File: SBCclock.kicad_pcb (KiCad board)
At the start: 4 copper layers, 37.5 x 23.4 mm, 20 parts, among them J1 Conn_01x07, J2 Conn_01x07, U1 74HCT14, U2 74HCT163, U3 74HCT112, U5 74HCT153, Y1 25.175MHz

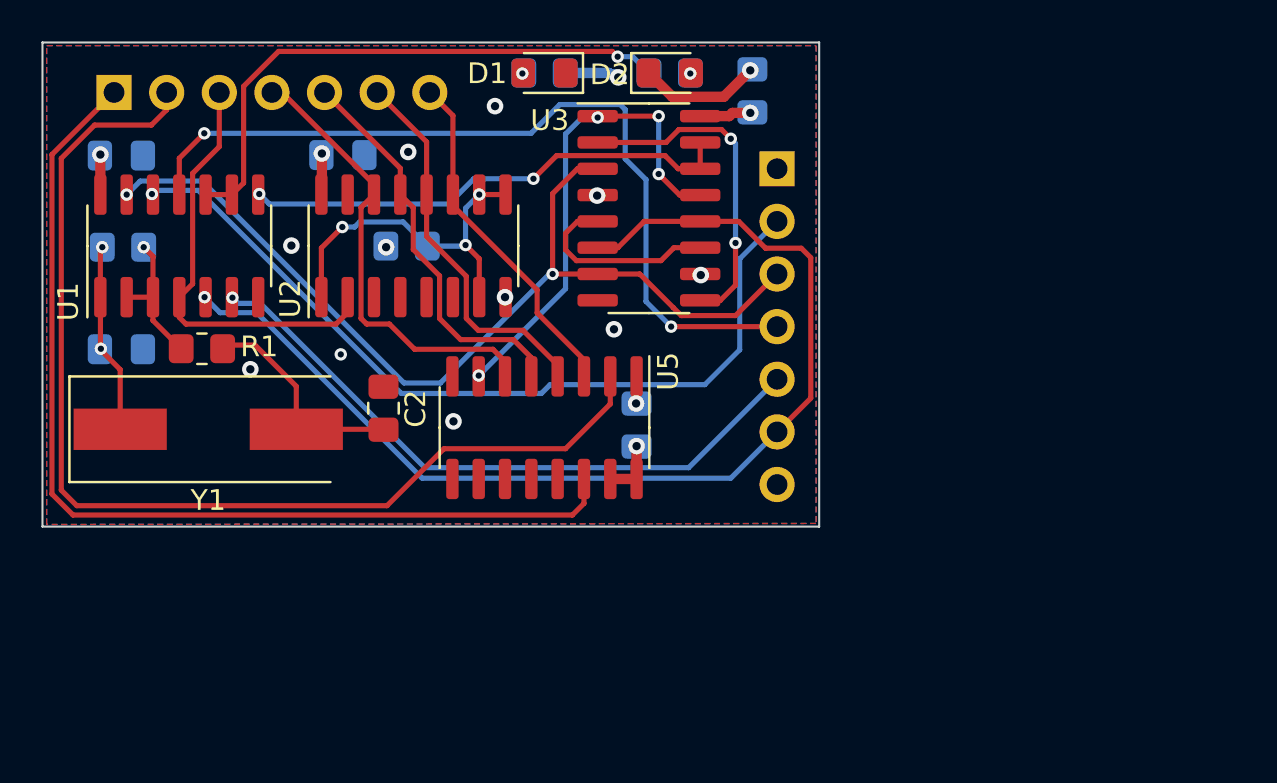
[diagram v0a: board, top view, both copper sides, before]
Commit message: reinforce clock outputs
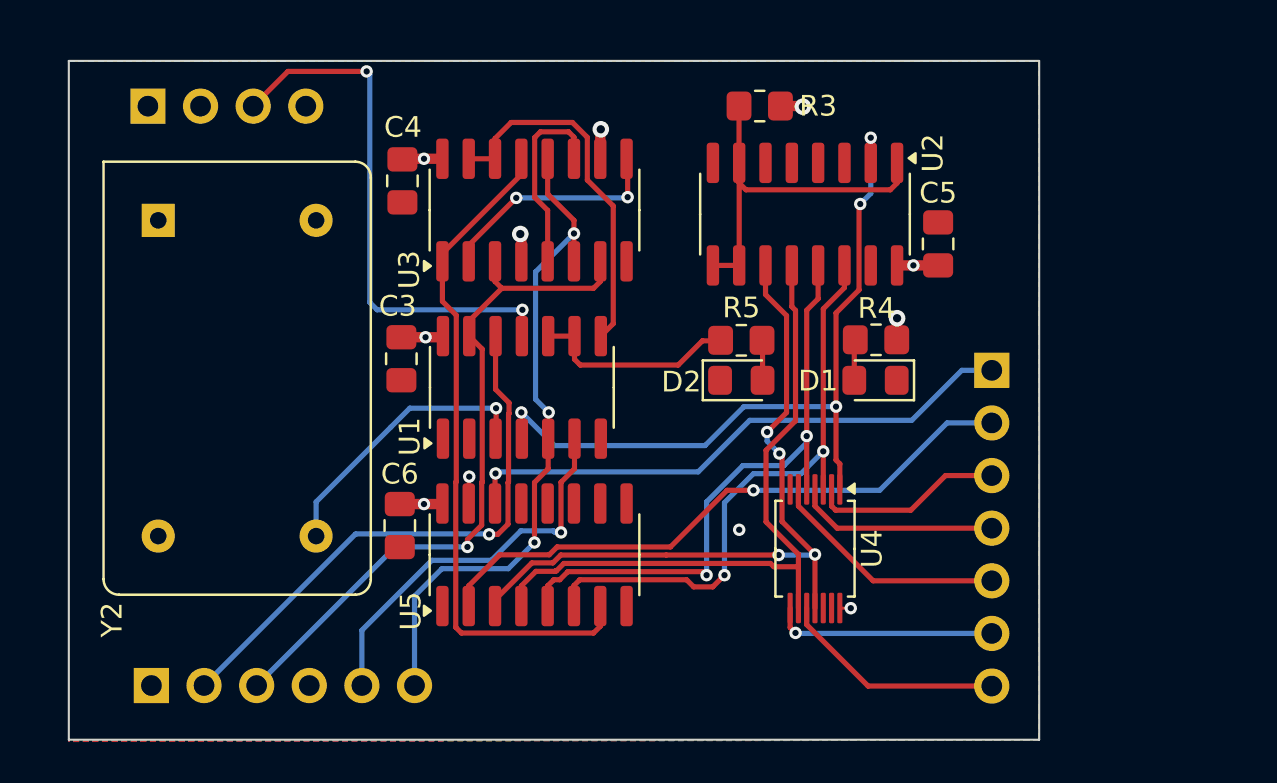
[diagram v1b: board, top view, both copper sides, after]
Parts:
- removed C1, C2: 4.7pF, Capacitor_SMD:C_0805_2012Metric_Pad1.18x1.45mm_HandSolder
- removed R1: 1K, Resistor_SMD:R_0805_2012Metric_Pad1.20x1.40mm_HandSolder
- removed R2: 1M, Resistor_SMD:R_0805_2012Metric_Pad1.20x1.40mm_HandSolder
- removed Y1: 25.175MHz, Crystal:Crystal_SMD_HC49-SD
- added J3: power, Connector_PinHeader_2.54mm:PinHeader_1x04_P2.54mm_Vertical, B.Cu at (148.1, 63.1)
- added U4: 74ACT07, Package_SO:TSSOP-14_4.4x3.6mm_P0.4mm, F.Cu at (180.3, 84.4)
- added Y2: GTXO-S14V, Oscillator:Oscillator_DIP-14, F.Cu at (148.6, 68.6)
- C3, C4, C5, C6, R3, R4, R5: moved to F.Cu
- J1: value Conn_01x07 -> clocks
- J2: value Conn_01x07 -> quadrature; footprint Connector_PinHeader_2.54mm:PinHeader_1x07_P2.54mm_Vertical -> Connector_PinHeader_2.54mm:PinHeader_1x06_P2.54mm_Vertical
- moved J1 44.4 mm to (188.8, 75.8), turned to 180 degrees
- moved J2 39.2 mm to (148.3, 91.0), turned to -90 degrees
- moved C5 29.0 mm to (186.2, 69.7), turned to 90 degrees
- moved D1 21.8 mm to (183.2, 76.3)
- moved R4 20.5 mm to (183.2, 74.3)
- moved U2 19.0 mm to (179.8, 68.3), turned to -90 degrees
- moved R3 18.3 mm to (177.6, 63.1), turned to 180 degrees
- moved U1 17.9 mm to (166.1, 76.6)
- moved C4 17.4 mm to (160.4, 66.7), turned to -90 degrees
- moved C3 16.7 mm to (160.3, 75.3), turned to -90 degrees
- moved D2 15.2 mm to (176.7, 76.3)
- moved R5 13.4 mm to (176.7, 74.4)
- moved C6 12.4 mm to (160.2, 83.3), turned to -90 degrees
- moved U5 6.15 mm to (166.8, 84.7), turned to 90 degrees
- moved U3 5.52 mm to (166.8, 68.1), turned to 90 degrees
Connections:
- J1 pad 3: Clock24 -> Net-(J1-Pin_3)
- J1 pad 4: Clock12 -> Net-(J1-Pin_4)
- J1 pad 5: Clock6 -> Net-(J1-Pin_5)
- J1 pad 6: Clock3 -> Net-(J1-Pin_6)
- J1 pad 7: Clock1.5 -> Net-(J1-Pin_7)
- J2 pad 4: ~{RESET} -> unconnected-(J2-Pin_4-Pad4)
- U1 pad 1: Net-(C1-Pad2) -> unconnected-(U1-Pad1)
- U1 pad 2: Net-(R1-Pad2) -> unconnected-(U1-Pad2)
- U1 pad 3: Net-(R1-Pad2) -> Net-(Y2-OUT)
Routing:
- net SEL1: track 53.1 -> 29.5 mm, vias 0 -> 1
- net SEL0: track 48.1 -> 27.5 mm, vias 0 -> 1
- net ~{Q}: track 52.8 -> 32.9 mm, vias 1 -> 3
- net Clock1.5: track 16.8 -> 35.0 mm, vias 0 -> 4
- net RESET: track 27.4 -> 10.0 mm, vias 1 -> 0
- net Clock24: track 20.9 -> 36.9 mm, vias 0 -> 4
- net ~{RESET}: track 41.4 -> 26.2 mm
- net Clock3: track 18.6 -> 32.7 mm
- net Net-(Y2-OUT): track 0.00 -> 13.7 mm, vias 0 -> 1
- net E: track 40.3 -> 27.3 mm
- net Q: track 31.5 -> 19.1 mm
- net ~{E}: track 46.1 -> 33.9 mm, vias 2 -> 1
- net Net-(J1-Pin_5): track 0.00 -> 11.6 mm
- net Net-(J1-Pin_7): track 0.00 -> 11.0 mm
- net Net-(J1-Pin_6): track 0.00 -> 10.8 mm, vias 0 -> 1
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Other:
- board size 37.5 x 23.4 mm -> 46.8 x 32.8 mm

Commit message: revised board - tested
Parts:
- added D3: RED, LED_SMD:LED_0805_2012Metric_Pad1.15x1.40mm_HandSolder, F.Cu at (190.0, 88.6)
- added D4: YELLOW, LED_SMD:LED_0805_2012Metric_Pad1.15x1.40mm_HandSolder, F.Cu at (187.2, 88.6)
- added D5: GREEN, LED_SMD:LED_0805_2012Metric_Pad1.15x1.40mm_HandSolder, F.Cu at (184.5, 88.6)
- added R2: 330R, Resistor_SMD:R_0805_2012Metric_Pad1.20x1.40mm_HandSolder, F.Cu at (193.2, 89.6)
- added R8: 330R, Resistor_SMD:R_0805_2012Metric_Pad1.20x1.40mm_HandSolder, F.Cu at (188.2, 91.8)
- added R9: 330R, Resistor_SMD:R_0805_2012Metric_Pad1.20x1.40mm_HandSolder, F.Cu at (183.4, 91.7)
- added SW1: SW_Push, Button_Switch_SMD:SW_SPST_B3S-1000, F.Cu at (191.2, 76.4)
- added U6: DS1813, Package_TO_SOT_SMD:SOT-23-3, F.Cu at (186.3, 82.7)
- added U7: 74AHC1G14, Package_TO_SOT_SMD:SOT-353_SC-70-5_Handsoldering, F.Cu at (189.6, 82.9)
- J1: footprint Connector_PinHeader_2.54mm:PinHeader_1x07_P2.54mm_Vertical -> Connector_PinHeader_2.54mm:PinHeader_1x08_P2.54mm_Vertical
- J2: footprint Connector_PinHeader_2.54mm:PinHeader_1x06_P2.54mm_Vertical -> Connector_PinHeader_2.54mm:PinHeader_1x04_P2.54mm_Vertical
- moved J1 9.89 mm to (198.4, 73.3)
- moved J2 2.54 mm to (150.8, 91.0)
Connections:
- J2 pad 1: GND -> E
- J2 pad 2: E -> ~{E}
- J2 pad 3: ~{E} -> Q
- J2 pad 4: unconnected-(J2-Pin_4-Pad4) -> ~{Q}
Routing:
- net ~{RESET}: track 26.2 -> 94.8 mm
- net Net-(J1-Pin_6): track 10.8 -> 21.4 mm
- net Net-(J1-Pin_5): track 11.6 -> 22.2 mm, vias 0 -> 1
- net Net-(J1-Pin_3): track 9.31 -> 19.9 mm, vias 0 -> 1
- net Net-(J1-Pin_4): track 9.78 -> 20.4 mm, vias 0 -> 1
- net SEL1: track 29.5 -> 40.1 mm
- net Net-(J1-Pin_7): track 11.0 -> 21.6 mm, vias 0 -> 1
- net SEL0: track 27.5 -> 38.1 mm
- net +5V: track 14.8 -> 19.3 mm, vias 10 -> 12
- net Net-(D3-A): track 0.00 -> 3.73 mm
- net Net-(D3-K): track 0.00 -> 2.27 mm
- net Net-(D4-K): track 0.00 -> 2.18 mm
- net Net-(D5-K): track 0.00 -> 2.15 mm
- net Q: track 19.1 -> 20.1 mm
- net ~{Q}: track 32.9 -> 33.9 mm
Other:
- board size 46.8 x 32.8 mm -> 56.3 x 32.8 mm

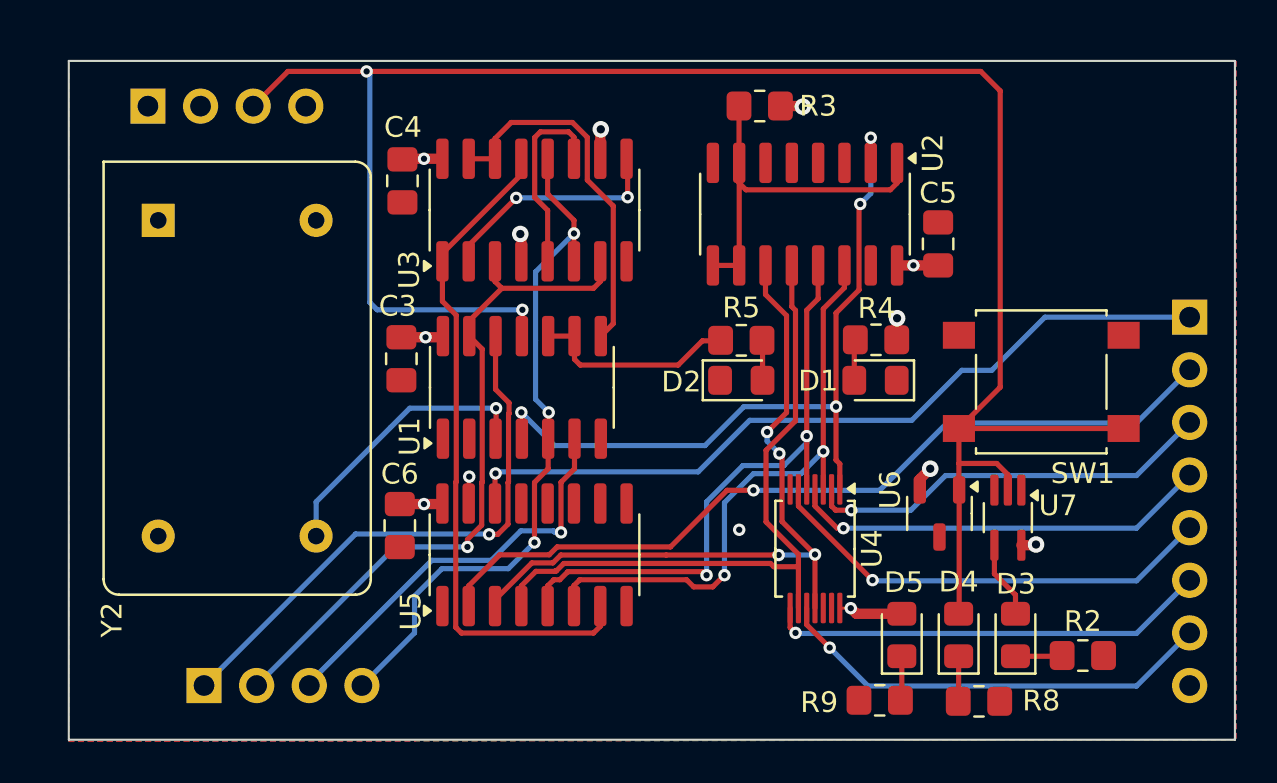
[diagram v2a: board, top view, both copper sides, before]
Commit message: remove redundant single gate
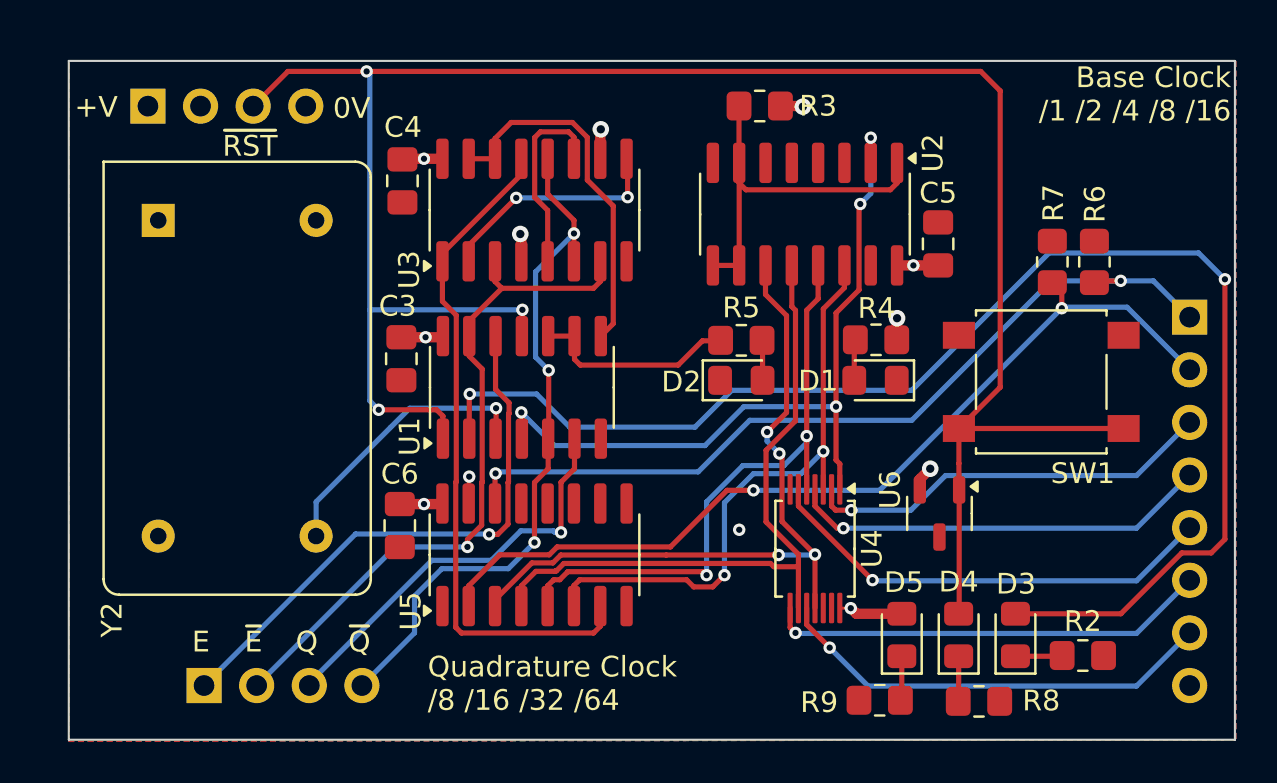
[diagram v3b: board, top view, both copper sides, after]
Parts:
- removed U7: 74AHC1G14, Package_TO_SOT_SMD:SOT-353_SC-70-5_Handsoldering
- added R6: 2.2k, Resistor_SMD:R_0805_2012Metric_Pad1.20x1.40mm_HandSolder, F.Cu at (193.8, 70.6)
- added R7: 2.2k, Resistor_SMD:R_0805_2012Metric_Pad1.20x1.40mm_HandSolder, F.Cu at (191.7, 70.6)
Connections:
- U1 pad 1: unconnected-(U1-Pad1) -> ~{RESET}
- U1 pad 2: unconnected-(U1-Pad2) -> Net-(D3-A)
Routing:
- net Net-(D3-A): track 3.73 -> 67.4 mm, vias 0 -> 2
- net ~{RESET}: track 94.8 -> 101.0 mm, vias 2 -> 3
- net SEL1: track 40.1 -> 44.0 mm, vias 1 -> 2
- net SEL0: track 38.1 -> 40.8 mm, vias 1 -> 2
- net +5V: track 19.3 -> 18.6 mm, vias 12 -> 11
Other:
- board text added: "+V"
- board text added: "0V"
- board text added: "Base Clock /1 /2 /4 /8 /16"
- board text added: "E"
- board text added: "Q"
- board text added: "Quadrature Clock /8 /16 /32 /64"
- board text added: "~{E}"
- board text added: "~{Q}"
- board text added: "~{RST}"

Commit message: update
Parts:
- removed D1, D2: LED, LED_SMD:LED_0805_2012Metric_Pad1.15x1.40mm_HandSolder
- removed R4, R5: 330R, Resistor_SMD:R_0805_2012Metric_Pad1.20x1.40mm_HandSolder
- SW1: value SW_Push -> RESET
- Y2: footprint Oscillator:Oscillator_DIP-14 -> Library:Oscillator_DIP-8+14
- moved U2 0.20 mm to (179.8, 68.1)
- moved C5 0.17 mm to (186.2, 69.5)
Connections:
- net Clock1.5 renamed Clock/16
- net Clock12 renamed Clock/2
- net Clock24 renamed ClockBase
- net Clock3 renamed Clock/8
- net Clock6 renamed Clock/4
- D3 pad 2: Net-(D3-A) -> RESET
- U1 pad 1: ~{RESET} -> GND
- U1 pad 2: Net-(D3-A) -> unconnected-(U1-Pad2)
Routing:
- net Net-(D3-A): track 67.4 -> 0.00 mm, vias 2 -> 0
- net RESET: track 10.0 -> 61.4 mm, vias 0 -> 2
- net ~{RESET}: track 101.0 -> 91.7 mm, vias 3 -> 2
- net Net-(Y2-OUT): track 13.7 -> 21.4 mm
- net Net-(J1-Pin_7): track 21.6 -> 25.2 mm, vias 1 -> 0
- net ClockBase: track 36.9 -> 38.6 mm
- net Net-(D2-A): track 1.40 -> 0.00 mm
- net +5V: track 18.6 -> 20.0 mm, vias 11 -> 10
- net Net-(D1-A): track 1.31 -> 0.00 mm
- net Clock/2: track 29.3 -> 30.1 mm
- net QuadC: track 32.7 -> 33.5 mm
- net Net-(J1-Pin_6): track 21.4 -> 22.1 mm
- net GND: vias 1 -> 23

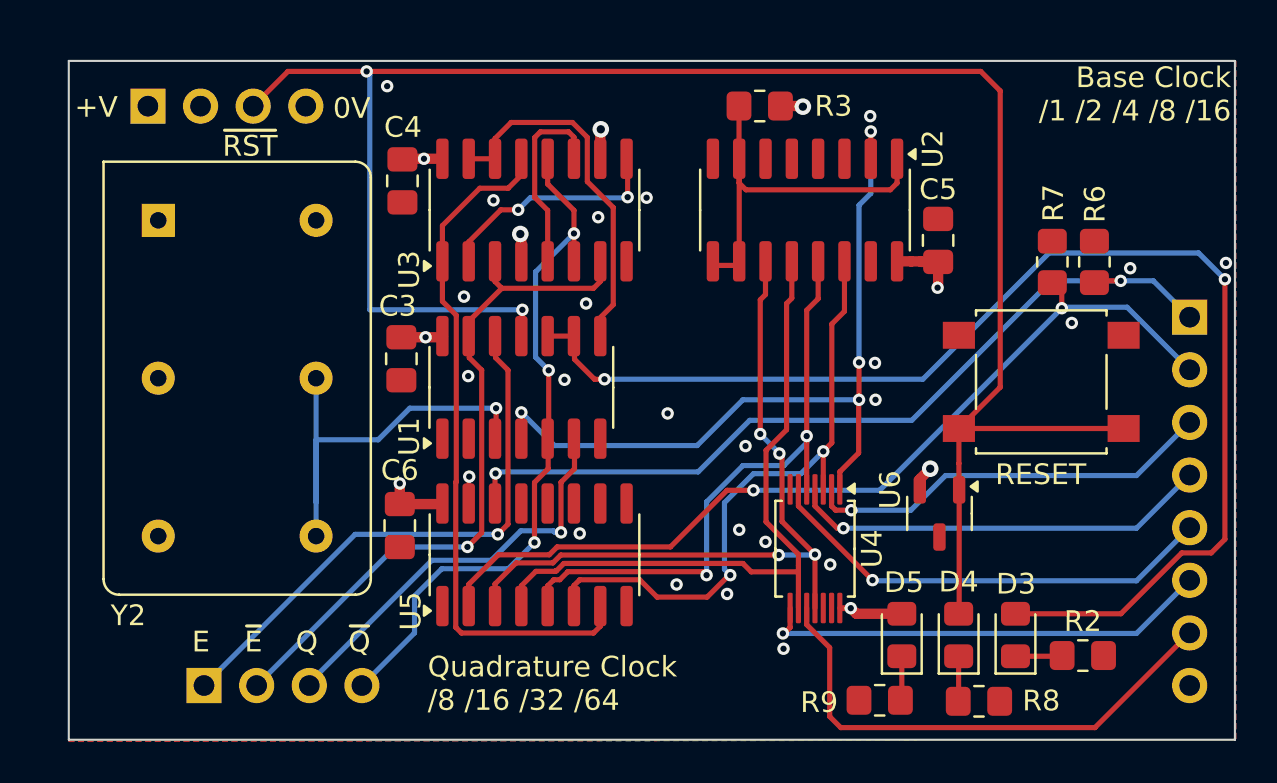
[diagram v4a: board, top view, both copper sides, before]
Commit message: fix u4 footprint
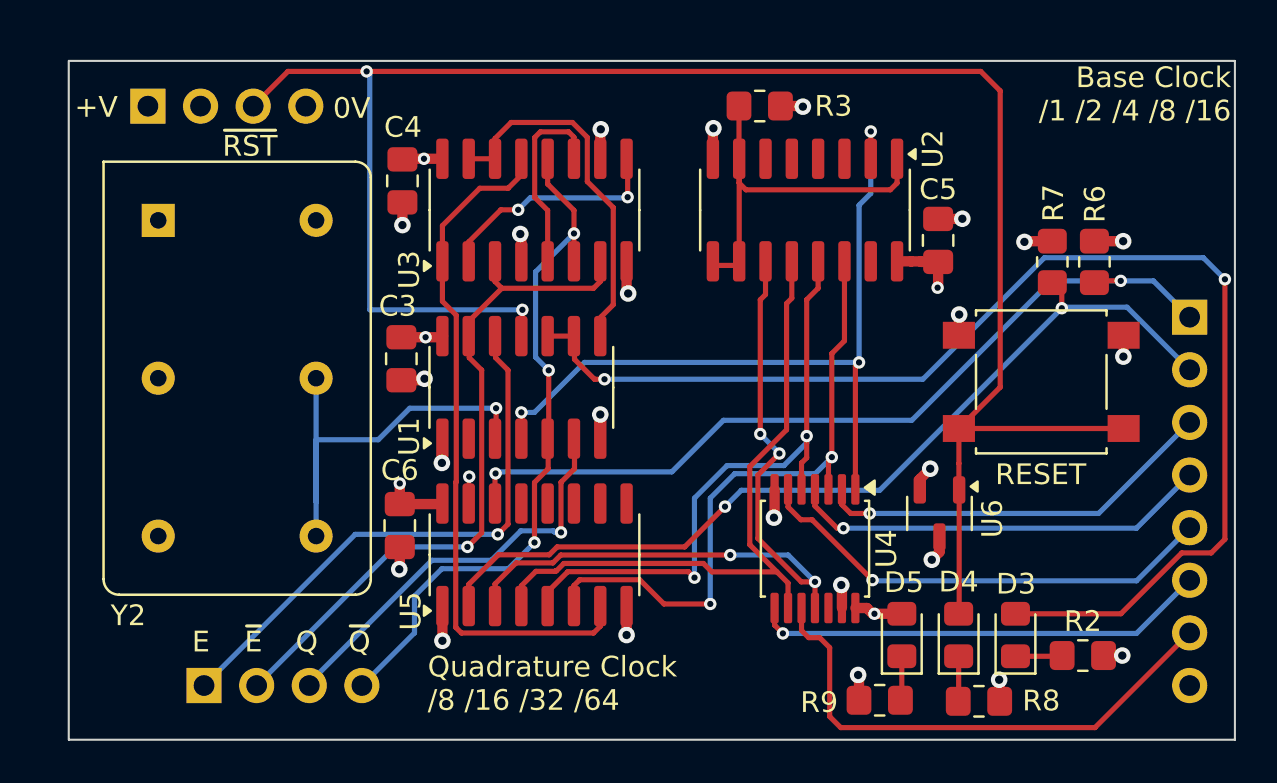
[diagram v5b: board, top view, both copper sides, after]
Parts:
- U4: value 74ACT07 -> 74ACT17; footprint Package_SO:TSSOP-14_4.4x3.6mm_P0.4mm -> Package_SO:TSSOP-14_4.4x5mm_P0.65mm
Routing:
- net GND: track 0.00 -> 24.7 mm, vias 23 -> 20
- net Clock/16: track 34.9 -> 36.8 mm
- net Clock/2: track 30.1 -> 31.2 mm
- net ClockBase: track 38.6 -> 37.7 mm, vias 4 -> 3
- net +5V: track 20.0 -> 19.2 mm
- net Clock/8: track 32.7 -> 32.1 mm
- net Net-(J1-Pin_5): track 22.2 -> 22.8 mm
- removed copper zone on B.Cu, net GND
- removed copper zone on F.Cu, net GND
